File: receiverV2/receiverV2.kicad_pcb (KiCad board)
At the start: 4 copper layers, 57 x 66 mm, 21 parts, among them J1 Raspberry_Pi_4, J2 S3B-PH-SM4-TB, J3 S2B-PH-SM4-TB, U1 Teensy4.0, U2 AP63205WU-7

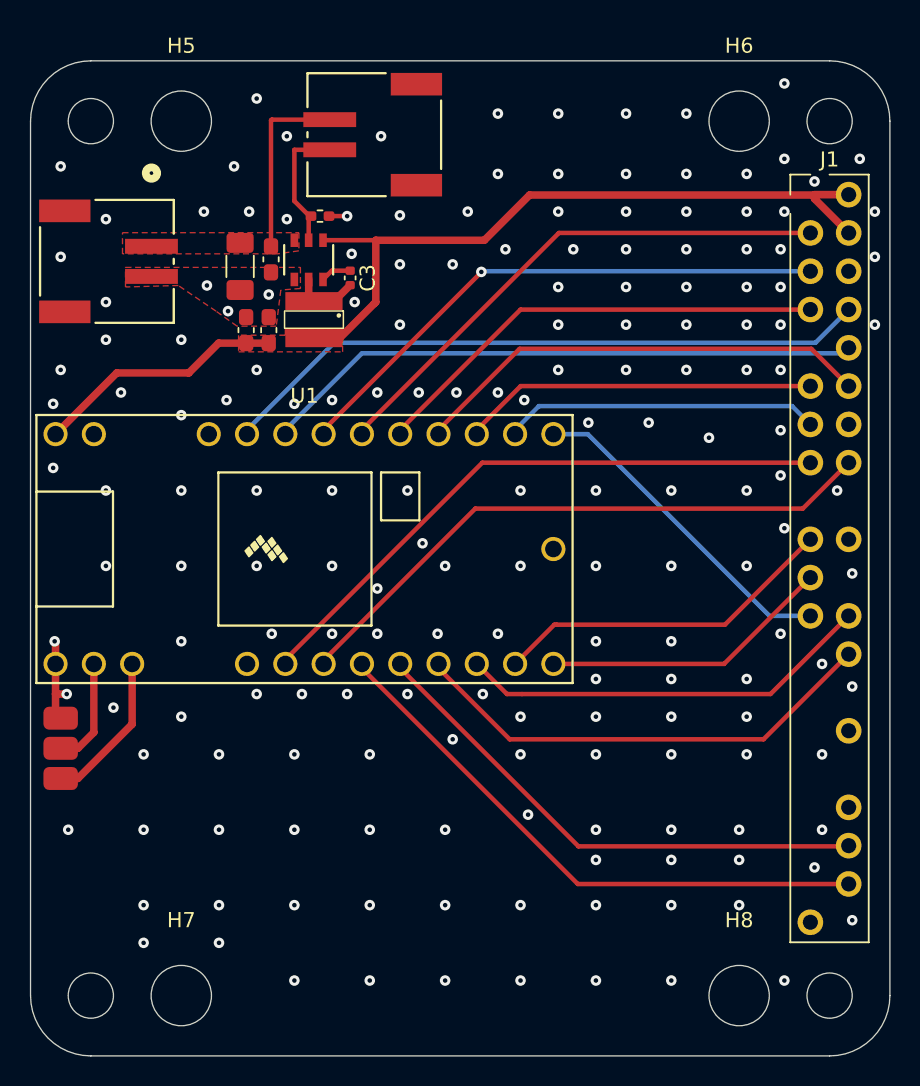
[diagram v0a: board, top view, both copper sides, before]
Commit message: add teensy4.1 version of receiver
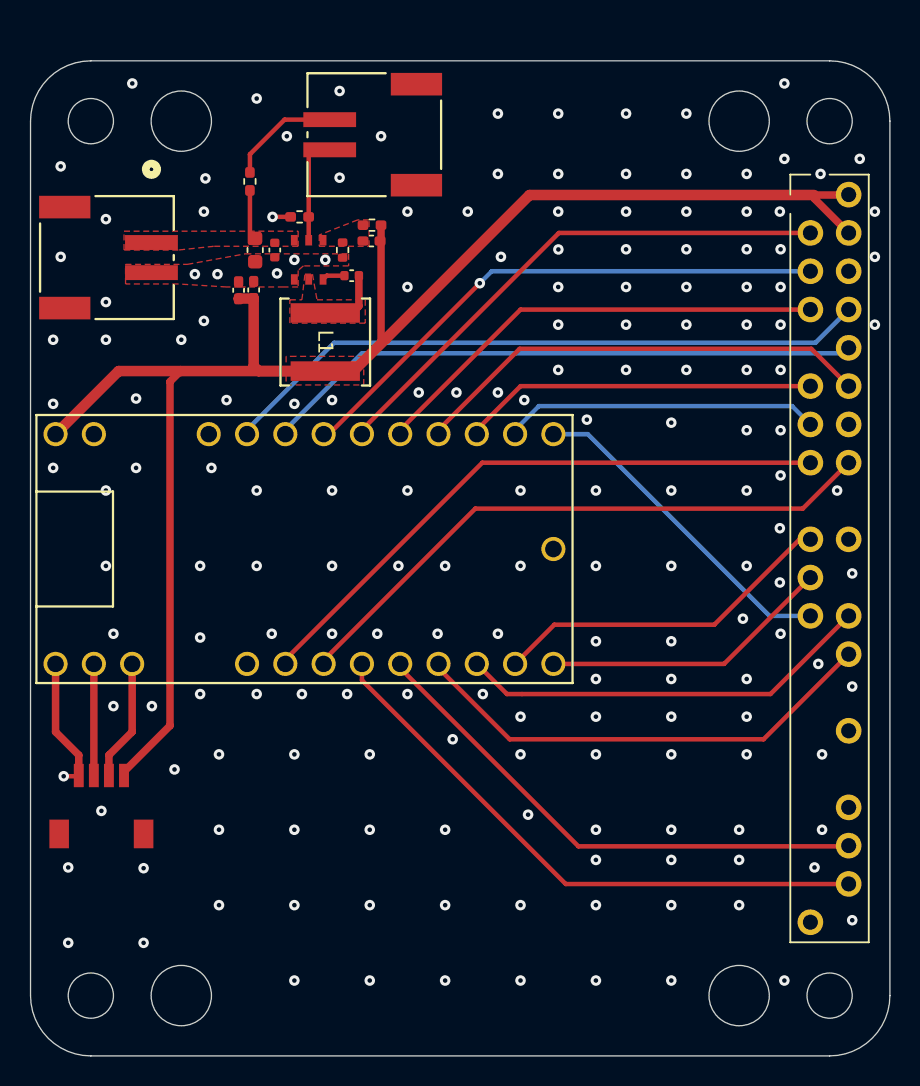
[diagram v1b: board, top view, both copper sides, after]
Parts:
- added C6: 47p, Capacitor_SMD:C_0402_1005Metric_Pad0.74x0.62mm_HandSolder, F.Cu at (78.6, 58.0)
- added R2: 100k, Resistor_SMD:R_0402_1005Metric_Pad0.72x0.64mm_HandSolder, F.Cu at (70.5, 54.0)
- added R3: 162k, Resistor_SMD:R_0402_1005Metric_Pad0.72x0.64mm_HandSolder, F.Cu at (78.7, 56.9)
- added R4: 31.1k, Resistor_SMD:R_0402_1005Metric, F.Cu at (76.7, 58.5)
- C1: footprint Capacitor_SMD:C_1206_3216Metric_Pad1.33x1.80mm_HandSolder -> Capacitor_SMD:C_0603_1608Metric
- C2: footprint Capacitor_SMD:C_0603_1608Metric_Pad1.08x0.95mm_HandSolder -> Capacitor_SMD:C_0402_1005Metric
- C4, C5: footprint Capacitor_SMD:C_0603_1608Metric_Pad1.08x0.95mm_HandSolder -> Capacitor_SMD:C_0402_1005Metric_Pad0.74x0.62mm_HandSolder
- J2: value S3B-PH-SM4-TB -> SM04B-SRSS-TB; footprint TF:3pin pad -> JST SH 4pin:CONN_SM04B-SRSS-TB_JST
- L1: value 5.6uH -> 6.8uH; footprint TF:WE-XHMI SMT Power Inductor 4040 -> Bourns_induct:IND_SRP5050FA-5R6M_BRN_mod
- R1: value R_Small_US -> 100k
- U2: value AP63205WU-7 -> AP63300WU-7_mod; footprint footprints:SOIC_05WU-7_DIO -> footprints:SOIC_05WU-7_DIO-L_mod
- moved J2 5.07 mm to (60.7, 95.5), turned to 180 degrees
- moved C4 2.84 mm to (70.8, 61.2)
- moved L1 2.81 mm to (75.5, 64.7)
- moved C5 2.69 mm to (69.8, 61.2)
- moved C1 1.48 mm to (70.9, 58.5)
- moved R1 1.35 mm to (73.8, 56.4), turned to 180 degrees
- moved C2 0.66 mm to (72.2, 58.5)
- moved J3 0.25 mm to (61.1, 59.0)
- moved C3 0.18 mm to (77.3, 60.2), turned to 0 degrees
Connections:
- J2 pad 1: /TX_ALT -> GND
- J2 pad 3: GND -> /TX_ALT
- On/Off/switch1 pad 2: VBUS -> Net-(On/Off/switch1-Pad2)
- U2 pad 1: +5V -> /FB
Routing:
- net +5V: track 65.4 -> 109.2 mm
- net VBUS: track 12.3 -> 3.47 mm
- net Net-(On/Off/switch1-Pad2): track 0.00 -> 7.45 mm
- net GND: track 7.21 -> 10.1 mm
- net /TX_ALT: track 10.2 -> 8.04 mm
- net /DC-DC-Out: track 4.42 -> 2.70 mm
- net /Enable: track 8.73 -> 7.39 mm
- net Net-(U2-BST): track 2.04 -> 1.52 mm
- added copper zone on F.Cu, net /DC-DC-Out
- added copper zone on F.Cu, net /FB
